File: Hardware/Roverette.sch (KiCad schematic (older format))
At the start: 4 parts, among them M1 Motor_DC, M2 Motor_DC

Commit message: Signed-off-by: Usman <usmanmehmood55@gmail.com>
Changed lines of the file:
@@
 Wire Wire Line
 	3900 2650 3850 2650
-Text Label 3900 2650 0    50   ~ 0
-VBAT
 Text Label 3250 2650 0    20   ~ 0
 `bat
 Connection ~ 3900 2650
-Wire Wire Line
-	3900 2650 3900 5000
 Text Label 6150 5000 0    20   ~ 0
 iPROPI_R
@@
 MR-
 $Comp
-L power:Vdrive #PWR0101
+L power:Vdrive #PWR02
 U 1 1 5FF4E8AF
 P 6100 2750
-F 0 "#PWR0101" H 5900 2600 50  0001 C CNN
+F 0 "#PWR02" H 5900 2600 50  0001 C CNN
 F 1 "Vdrive" V 6115 2878 50  0000 L CNN
 F 2 "" H 6100 2750 50  0001 C CNN
@@
 	0    1    1    0
 $EndComp
+Wire Wire Line
+	3900 2650 3900 5000
+Wire Wire Line
+	3900 2600 3900 2650
+$Comp
+L power:PWR_FLAG #FLG0101
+U 1 1 60713458
+P 3900 2600
+F 0 "#FLG0101" H 3900 2675 50  0001 C CNN
+F 1 "PWR_FLAG" V 3900 2728 50  0001 L CNN
+F 2 "" H 3900 2600 50  0001 C CNN
+F 3 "~" H 3900 2600 50  0001 C CNN
+	1    3900 2600
+	1    0    0    -1
+$EndComp
+Text Label 3900 2650 0    50   ~ 0
+VBAT
+$Comp
+L power:PWR_FLAG #FLG0102
+U 1 1 60715D09
+P 3250 3050
+F 0 "#FLG0102" H 3250 3125 50  0001 C CNN
+F 1 "PWR_FLAG" V 3250 3178 50  0001 L CNN
+F 2 "" H 3250 3050 50  0001 C CNN
+F 3 "~" H 3250 3050 50  0001 C CNN
+	1    3250 3050
+	0    -1   -1   0
+$EndComp
+Connection ~ 3250 3050
 $EndSCHEMATC

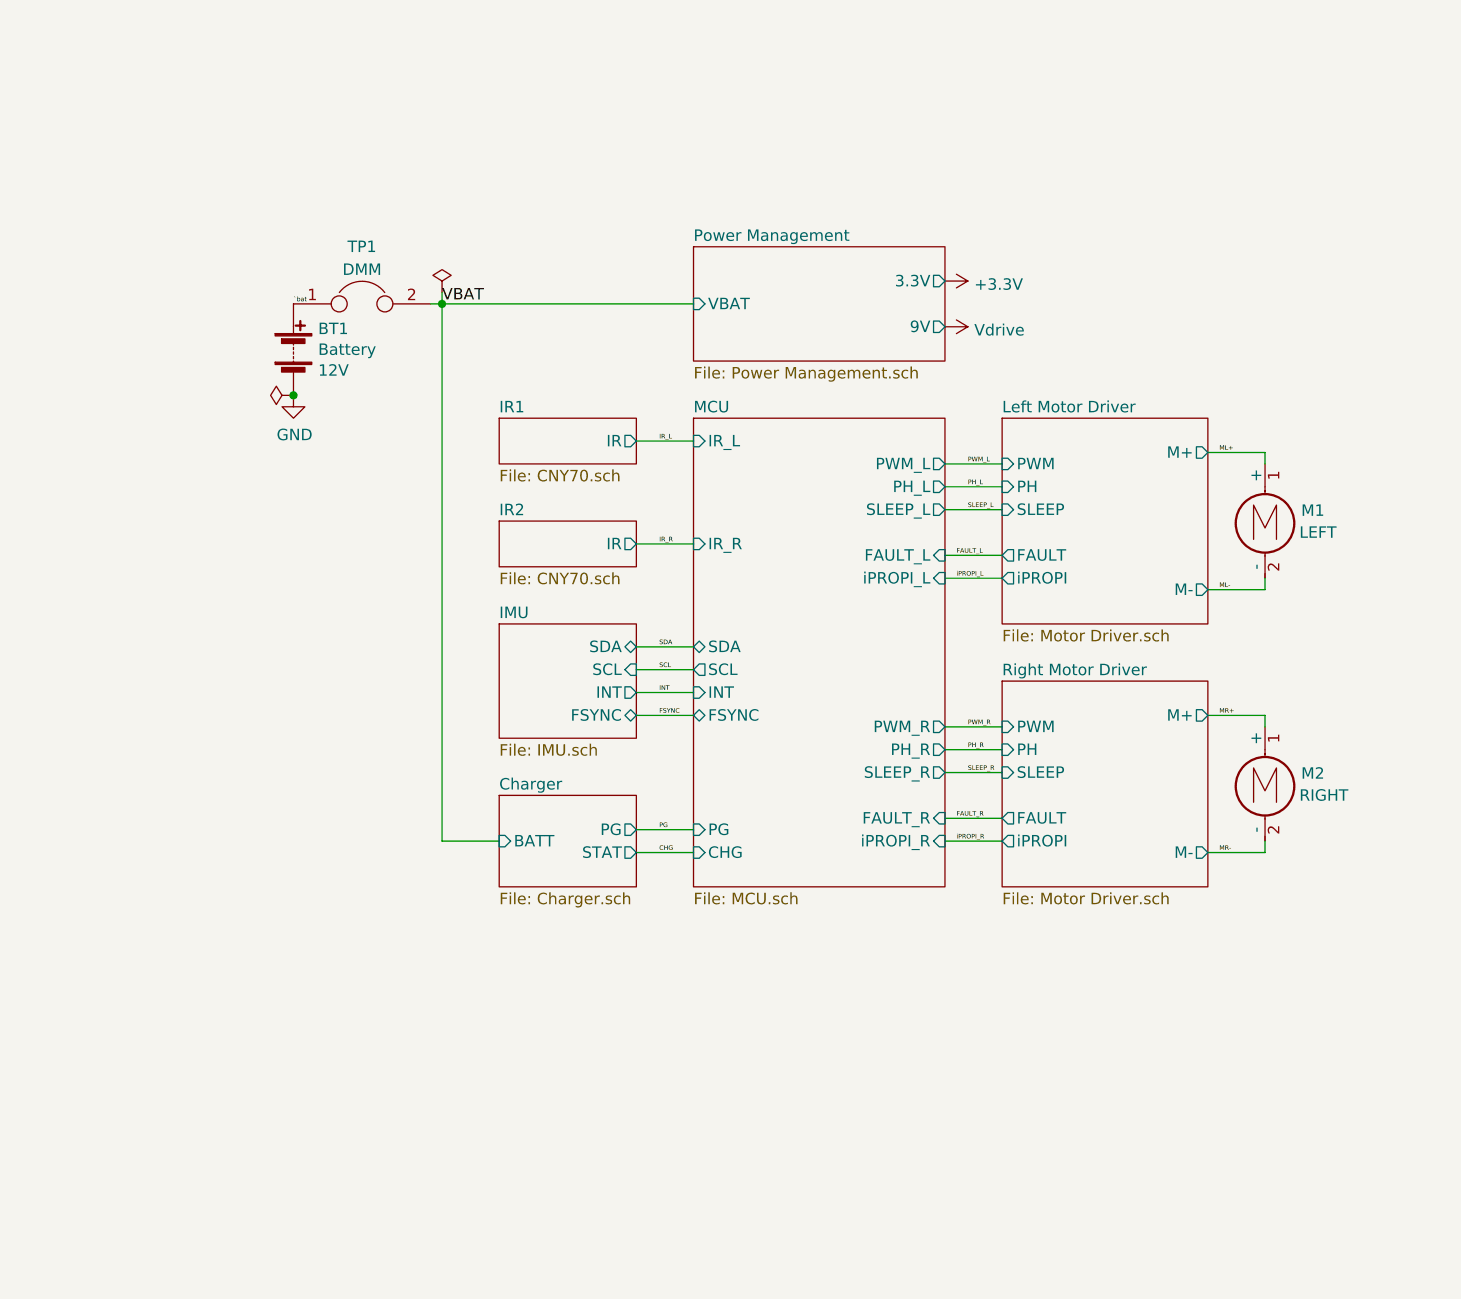
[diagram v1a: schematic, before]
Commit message: Schematic updated, USB comms circuit added
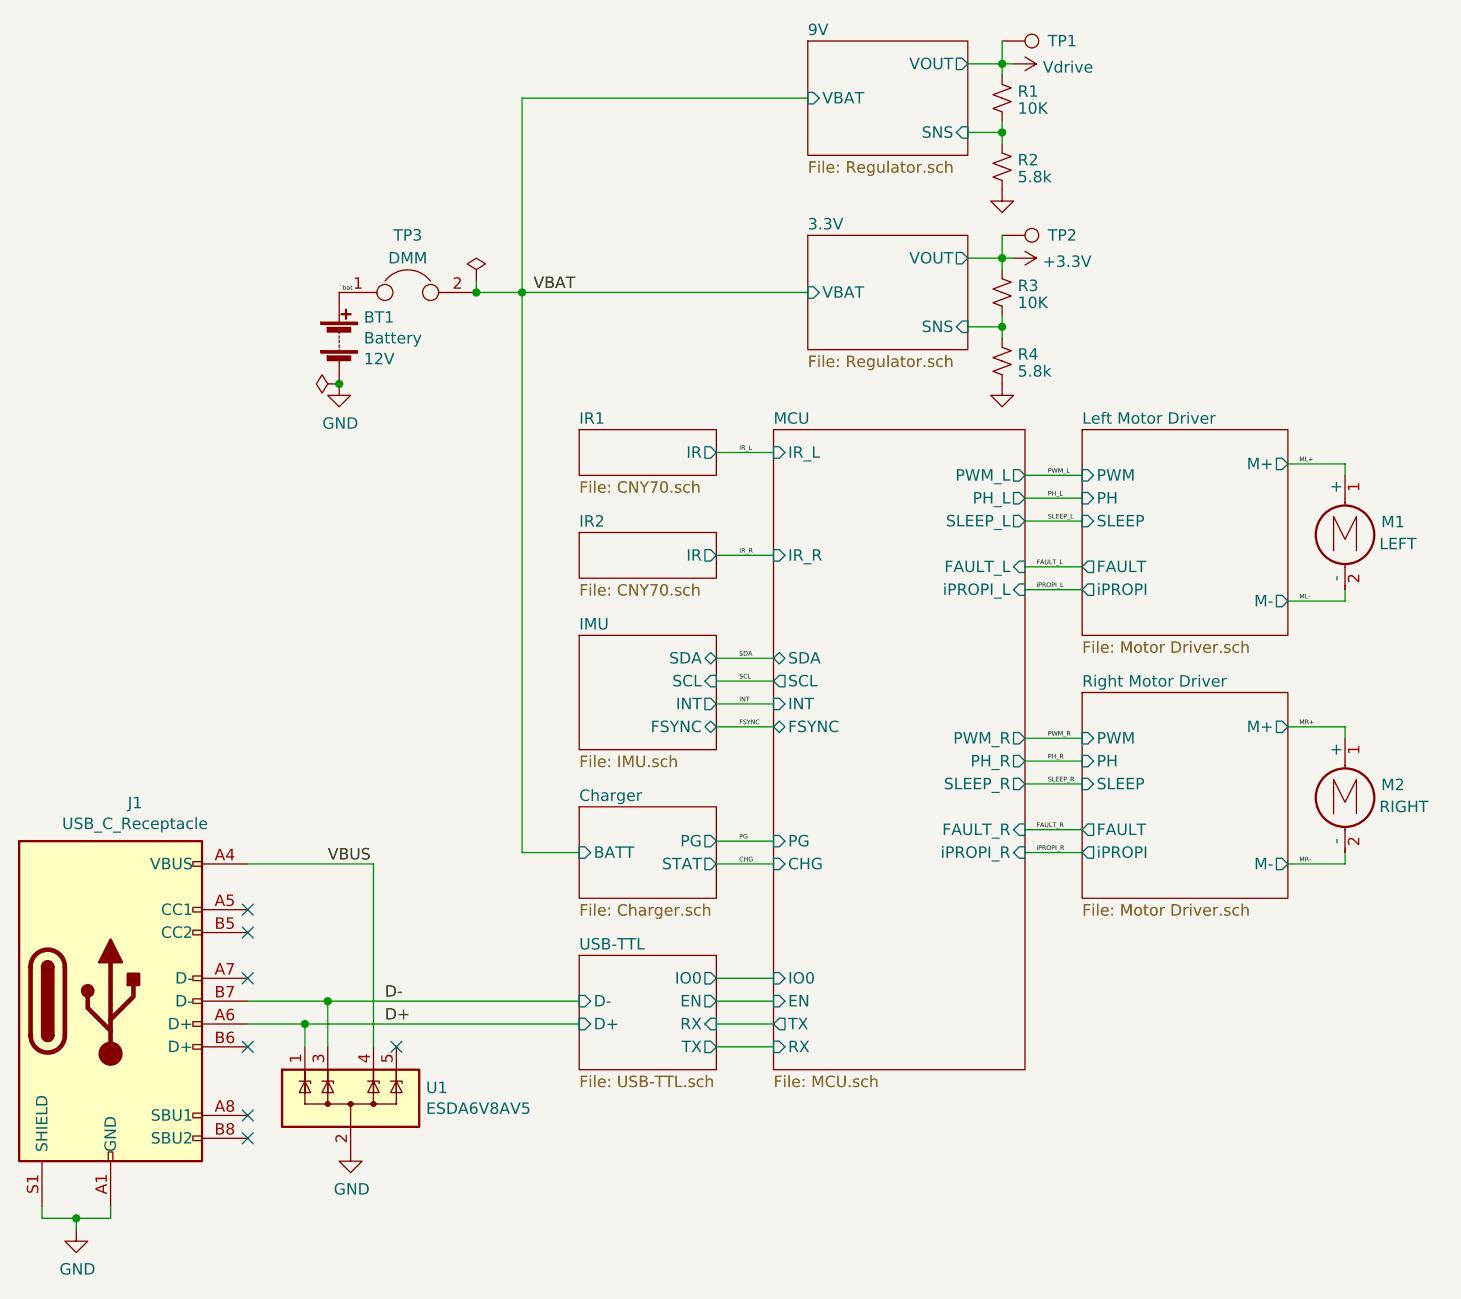
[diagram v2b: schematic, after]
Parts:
- added J1: USB_C_Receptacle, Connector_USB:USB_C_Receptacle_XKB_U262-16XN-4BVC11, symbol Connector:USB_C_Receptacle_USB2.0
- added R1, R3: 10K, Resistor_SMD:R_0805_2012Metric, symbol Device:R_Small_US
- added R2, R4: 5.8k, Resistor_SMD:R_0805_2012Metric, symbol Device:R_Small_US
- added TP1, TP2: TestPoint, TestPoint:TestPoint_Loop_D1.80mm_Drill1.0mm_Beaded, symbol Connector:TestPoint
- added U1: ESDA6V8AV5, Package_TO_SOT_SMD:SOT-553, symbol ESDA6V8AV5:ESDA6V8AV5
- BT1, M1, M2: footprint (none) -> TerminalBlock:TerminalBlock_bornier-2_P5.08mm
- renumbered TP1 to TP3
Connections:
- net +3V3: now also R3.1, TP2.1
- net GND: now also J1.A1 (GND), J1.A12 (GND), J1.B1 (GND), J1.B12 (GND), J1.S1 (SHIELD), R2.2, R4.2, U1.2
- net Vdrive: now also R1.1, TP1.1
- new net 3.3V/SNS: R3.2, R4.1
- new net 9V/SNS: R1.2, R2.1
- new net D+: J1.A6 (D+), U1.1
- new net D-: J1.B7 (D-), U1.3
- new net VBUS: J1.A4 (VBUS), J1.A9 (VBUS), J1.B4 (VBUS), J1.B9 (VBUS), U1.4
- no-connect marks 0 -> 7
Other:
- moved on the sheet: BT1, M1, M2, TP3

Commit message: Schematic and Readme updated
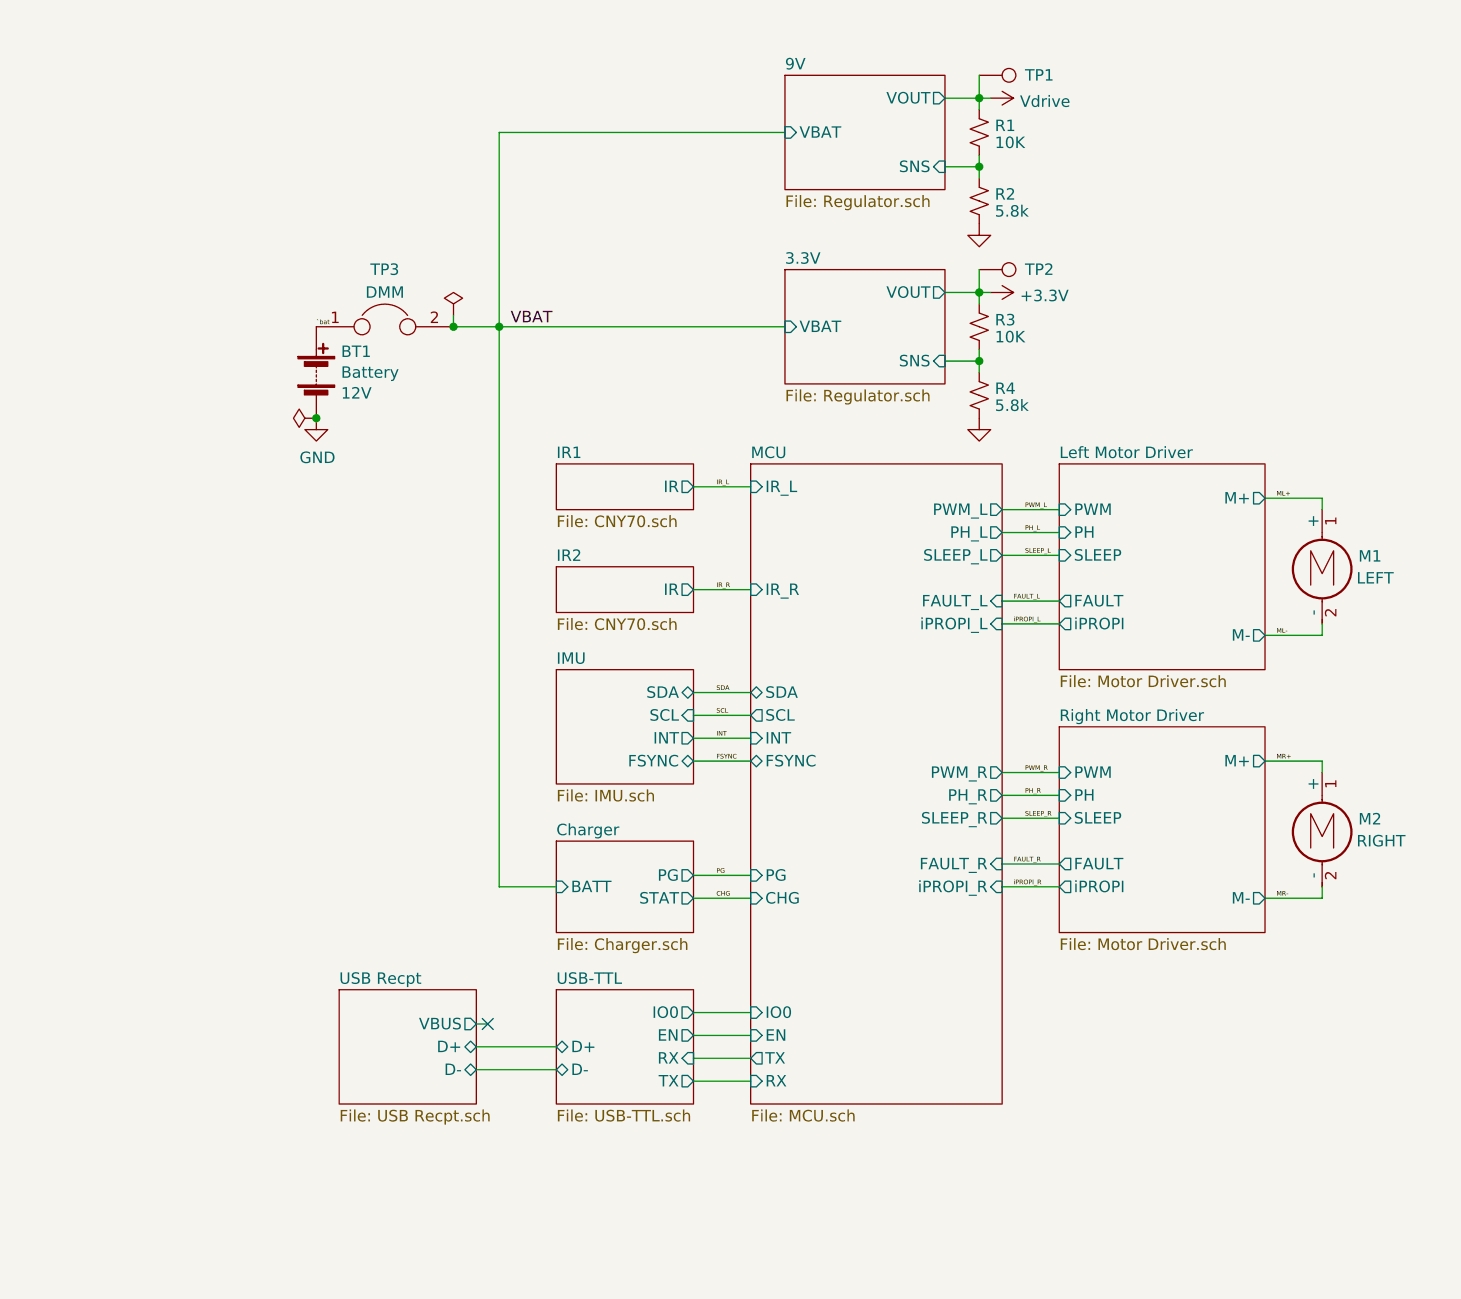
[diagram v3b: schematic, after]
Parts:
- removed J1: USB_C_Receptacle, Connector_USB:USB_C_Receptacle_XKB_U262-16XN-4BVC11, symbol Connector:USB_C_Receptacle_USB2.0
- removed U1: ESDA6V8AV5, Package_TO_SOT_SMD:SOT-553, symbol ESDA6V8AV5:ESDA6V8AV5
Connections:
- no-connect marks 7 -> 1
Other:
- moved on the sheet: BT1, M1, M2, R1, R2, R3, R4, TP1, TP2, TP3

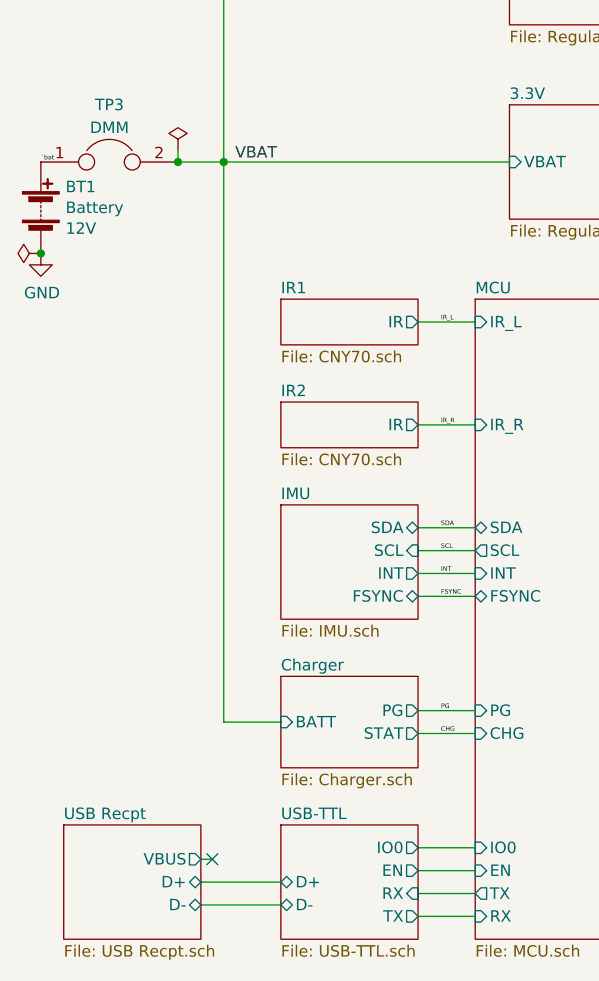
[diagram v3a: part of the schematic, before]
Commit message: vbus connected from USB to charger sheet
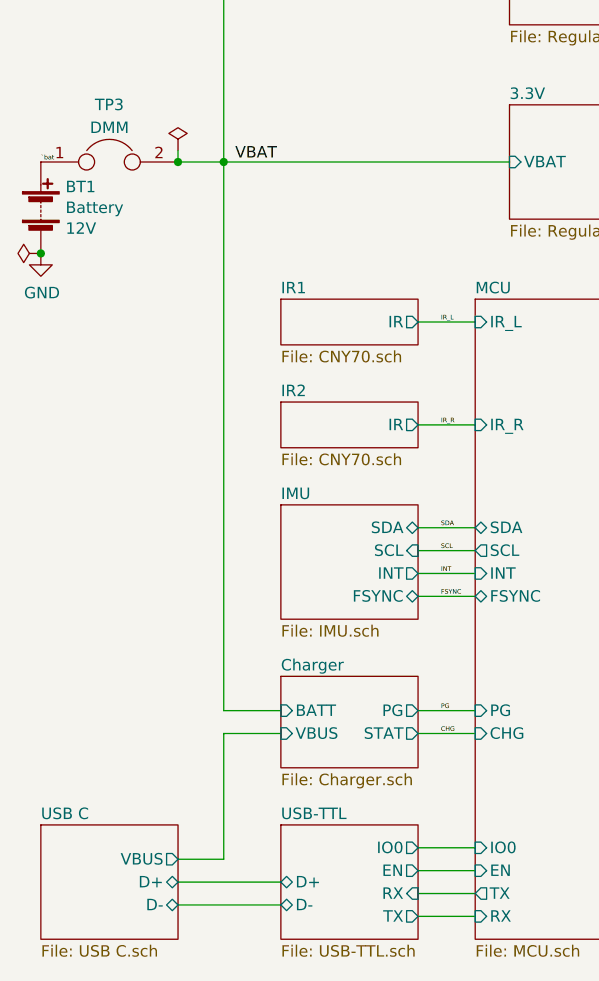
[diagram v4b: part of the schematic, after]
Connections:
- no-connect marks 1 -> 0
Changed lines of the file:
@@
 F1 "Charger.sch" 50
 F2 "PG" O R 5000 5150 50
-F3 "BATT" I L 4400 5200 50
+F3 "BATT" I L 4400 5150 50
 F4 "STAT" O R 5000 5250 50
-$EndSheet
-Wire Wire Line
-	4150 5200 4400 5200
+F5 "VBUS" I L 4400 5250 50
+$EndSheet
+Wire Wire Line
+	4150 5150 4400 5150
 Wire Wire Line
 	5000 3450 5250 3450
@@
 Connection ~ 4150 2750
 Wire Wire Line
-	4150 2750 4150 5200
+	4150 2750 4150 5150
 Wire Wire Line
 	4150 1900 4150 2750
@@
 Wire Wire Line
 	5000 6050 5250 6050
+Wire Wire Line
+	4150 5800 4150 5250
+Wire Wire Line
+	4150 5250 4400 5250
 $Sheet
-S 3450 5650 600  500
+S 3350 5650 600  500
 U 60893A6D
-F0 "USB Recpt" 50
-F1 "USB Recpt.sch" 50
-F2 "VBUS" O R 4050 5800 50
-F3 "D+" B R 4050 5900 50
-F4 "D-" B R 4050 6000 50
-$EndSheet
-Wire Wire Line
-	4050 5900 4400 5900
-Wire Wire Line
-	4050 6000 4400 6000
-Wire Wire Line
-	4050 5800 4100 5800
-NoConn ~ 4100 5800
+F0 "USB C" 50
+F1 "USB C.sch" 50
+F2 "VBUS" O R 3950 5800 50
+F3 "D+" B R 3950 5900 50
+F4 "D-" B R 3950 6000 50
+$EndSheet
+Wire Wire Line
+	3950 5800 4150 5800
+Wire Wire Line
+	3950 5900 4400 5900
+Wire Wire Line
+	3950 6000 4400 6000
 $EndSCHEMATC

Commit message: PCB design started
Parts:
- BT1: symbol Device:Battery -> Roverette-rescue:Battery-Device
- M1, M2: symbol Motor:Motor_DC -> Roverette-rescue:Motor_DC-Motor
- R1, R2, R3, R4: symbol Device:R_Small_US -> Roverette-rescue:R_Small_US-Device
- TP1: renamed from TP3; symbol Device:Jumper -> Roverette-rescue:Jumper-Device
- TP2: renamed from TP1; symbol Connector:TestPoint -> Roverette-rescue:TestPoint-Connector
- TP3: renamed from TP2; symbol Connector:TestPoint -> Roverette-rescue:TestPoint-Connector
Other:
- moved on the sheet: R1, R2, TP2

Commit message: Did placements and routing of one regulator
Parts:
- TP2: value TestPoint -> vDrive
- TP3: value TestPoint -> 3v3
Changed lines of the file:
@@
 AR Path="/6070D6A9" Ref="TP3"  Part="1"
 F 0 "TP3" V 6250 2700 50  0000 L CNN
-F 1 "TestPoint" H 6308 2527 50  0001 L CNN
+F 1 "3v3" H 6308 2527 50  0001 L CNN
 F 2 "TestPoint:TestPoint_Loop_D1.80mm_Drill1.0mm_Beaded" H 6450 2500 50  0001 C CNN
 F 3 "~" H 6450 2500 50  0001 C CNN
@@
 AR Path="/6082D663" Ref="TP2"  Part="1"
 F 0 "TP2" V 6250 1750 50  0000 L CNN
-F 1 "TestPoint" H 6308 1577 50  0001 L CNN
+F 1 "vDrive" H 6308 1577 50  0001 L CNN
 F 2 "TestPoint:TestPoint_Loop_D1.80mm_Drill1.0mm_Beaded" H 6450 1550 50  0001 C CNN
 F 3 "~" H 6450 1550 50  0001 C CNN
